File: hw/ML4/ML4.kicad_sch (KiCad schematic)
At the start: 4 parts

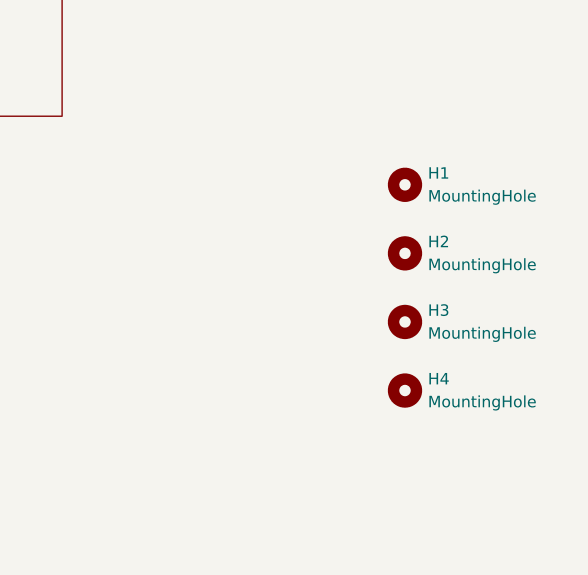
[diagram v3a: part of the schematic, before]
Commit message: Working on adding LCSC part numbers
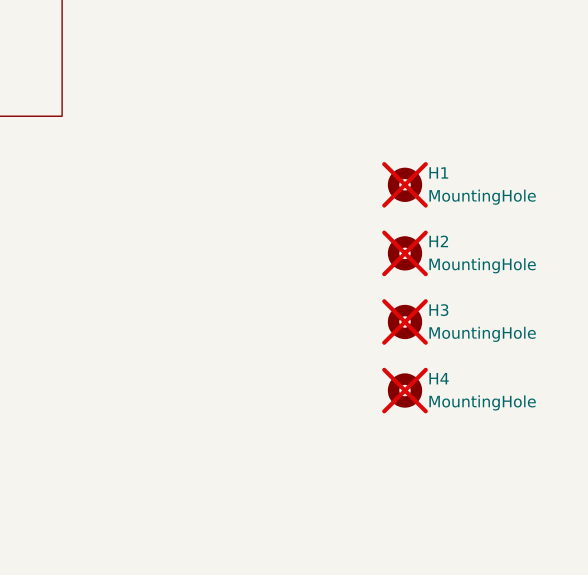
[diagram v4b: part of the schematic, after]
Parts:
- H1, H2, H3, H4: BOM Comments (none) -> No component, drill hole; now not fitted; now left out of the parts list
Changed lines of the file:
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@@
 		(unit 1)
 		(exclude_from_sim no)
-		(in_bom yes)
+		(in_bom no)
 		(on_board yes)
-		(dnp no)
+		(dnp yes)
 		(fields_autoplaced yes)
 		(property "Reference" "H1"
@@
 					(size 1.27 1.27)
 				)
+			)
+		)
+		(property "BOM Comments" "No component, drill hole"
+			(at 176.53 120.65 0)
+			(effects
+				(font
+					(size 1.27 1.27)
+				)
+				(hide yes)
+			)
+		)
+		(property "DK" ""
+			(at 176.53 120.65 0)
+			(effects
+				(font
+					(size 1.27 1.27)
+				)
+				(hide yes)
 			)
 		)
@@
 		(unit 1)
 		(exclude_from_sim no)
-		(in_bom yes)
+		(in_bom no)
 		(on_board yes)
-		(dnp no)
+		(dnp yes)
 		(fields_autoplaced yes)
 		(property "Reference" "H3"
@@
 					(size 1.27 1.27)
 				)
+			)
+		)
+		(property "BOM Comments" "No component, drill hole"
+			(at 176.53 135.89 0)
+			(effects
+				(font
+					(size 1.27 1.27)
+				)
+				(hide yes)
+			)
+		)
+		(property "DK" ""
+			(at 176.53 135.89 0)
+			(effects
+				(font
+					(size 1.27 1.27)
+				)
+				(hide yes)
 			)
 		)
@@
 		(unit 1)
 		(exclude_from_sim no)
-		(in_bom yes)
+		(in_bom no)
 		(on_board yes)
-		(dnp no)
+		(dnp yes)
 		(fields_autoplaced yes)
 		(property "Reference" "H2"
@@
 					(size 1.27 1.27)
 				)
+			)
+		)
+		(property "BOM Comments" "No component, drill hole"
+			(at 176.53 128.27 0)
+			(effects
+				(font
+					(size 1.27 1.27)
+				)
+				(hide yes)
+			)
+		)
+		(property "DK" ""
+			(at 176.53 128.27 0)
+			(effects
+				(font
+					(size 1.27 1.27)
+				)
+				(hide yes)
 			)
 		)
@@
 		(unit 1)
 		(exclude_from_sim no)
-		(in_bom yes)
+		(in_bom no)
 		(on_board yes)
-		(dnp no)
+		(dnp yes)
 		(fields_autoplaced yes)
 		(property "Reference" "H4"
@@
 			)
 		)
+		(property "BOM Comments" "No component, drill hole"
+			(at 176.53 143.51 0)
+			(effects
+				(font
+					(size 1.27 1.27)
+				)
+				(hide yes)
+			)
+		)
+		(property "DK" ""
+			(at 176.53 143.51 0)
+			(effects
+				(font
+					(size 1.27 1.27)
+				)
+				(hide yes)
+			)
+		)
